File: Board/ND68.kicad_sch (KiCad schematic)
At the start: 4 parts

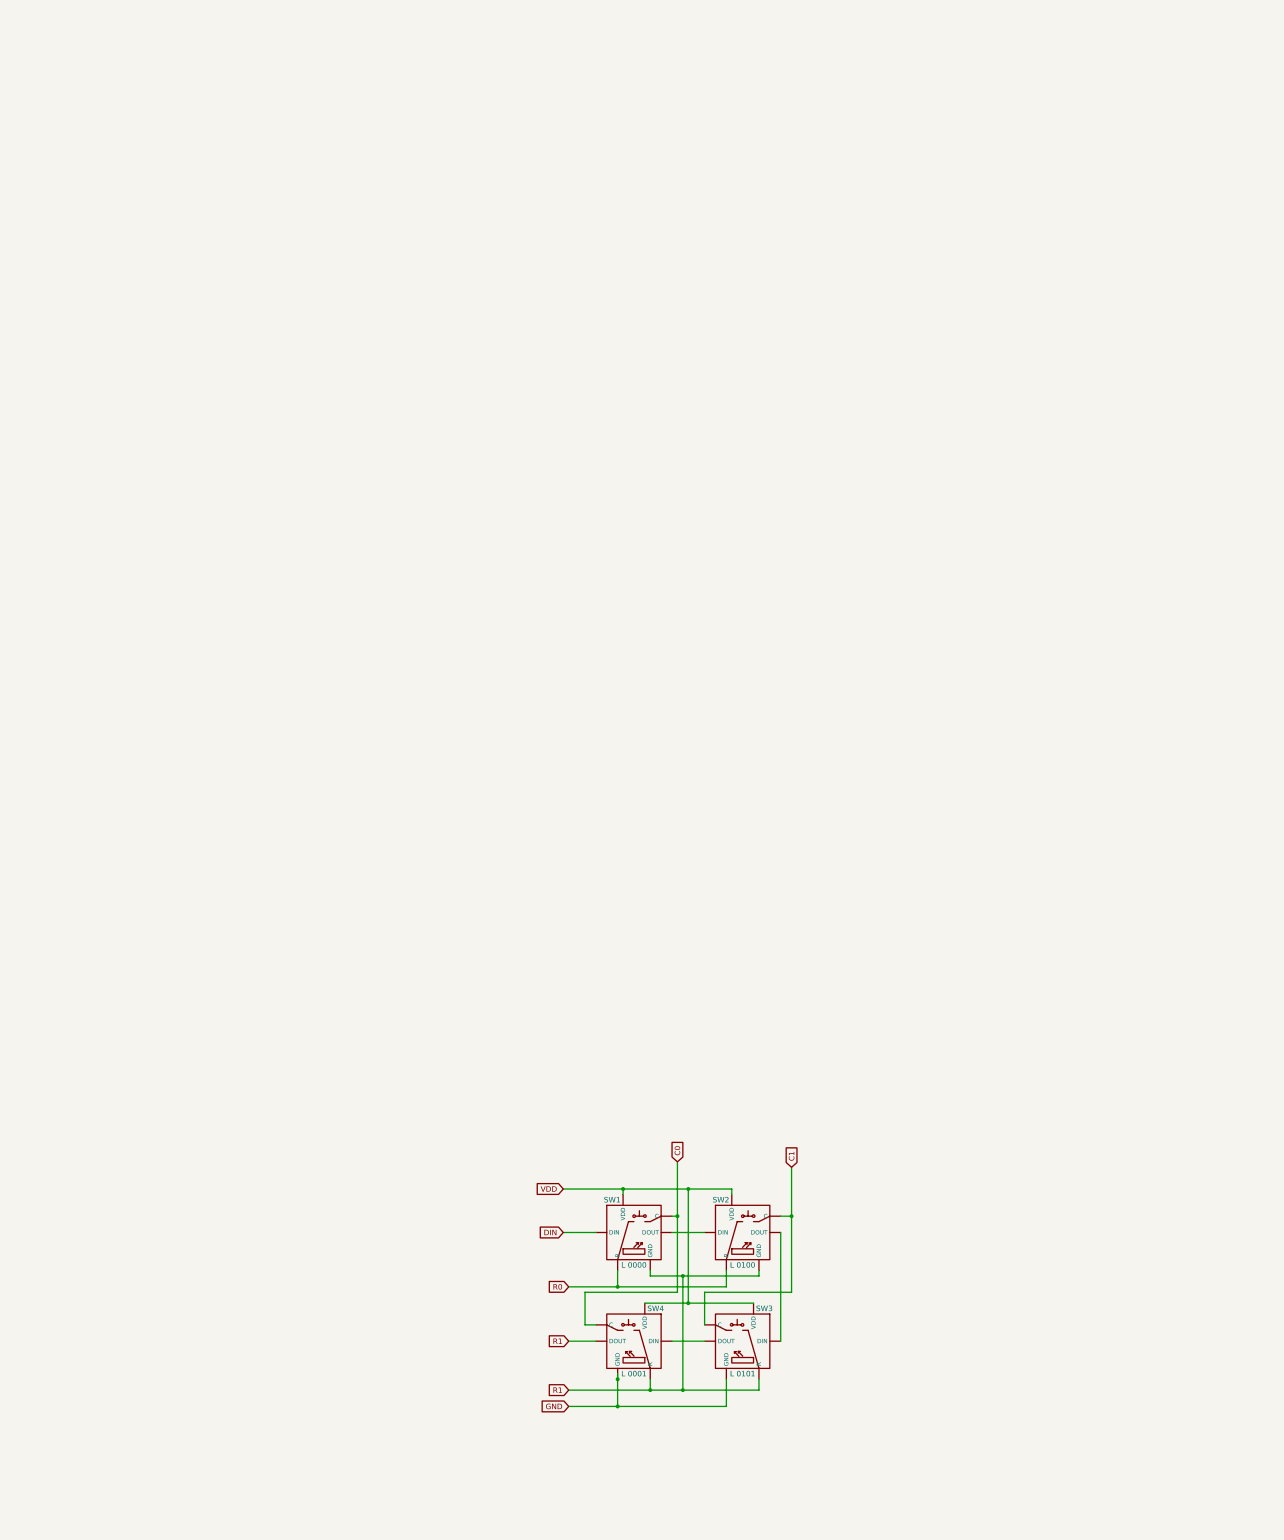
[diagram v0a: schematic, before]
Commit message: Added schematics, footprints, 3d models, and wiring to rp2040 input supply
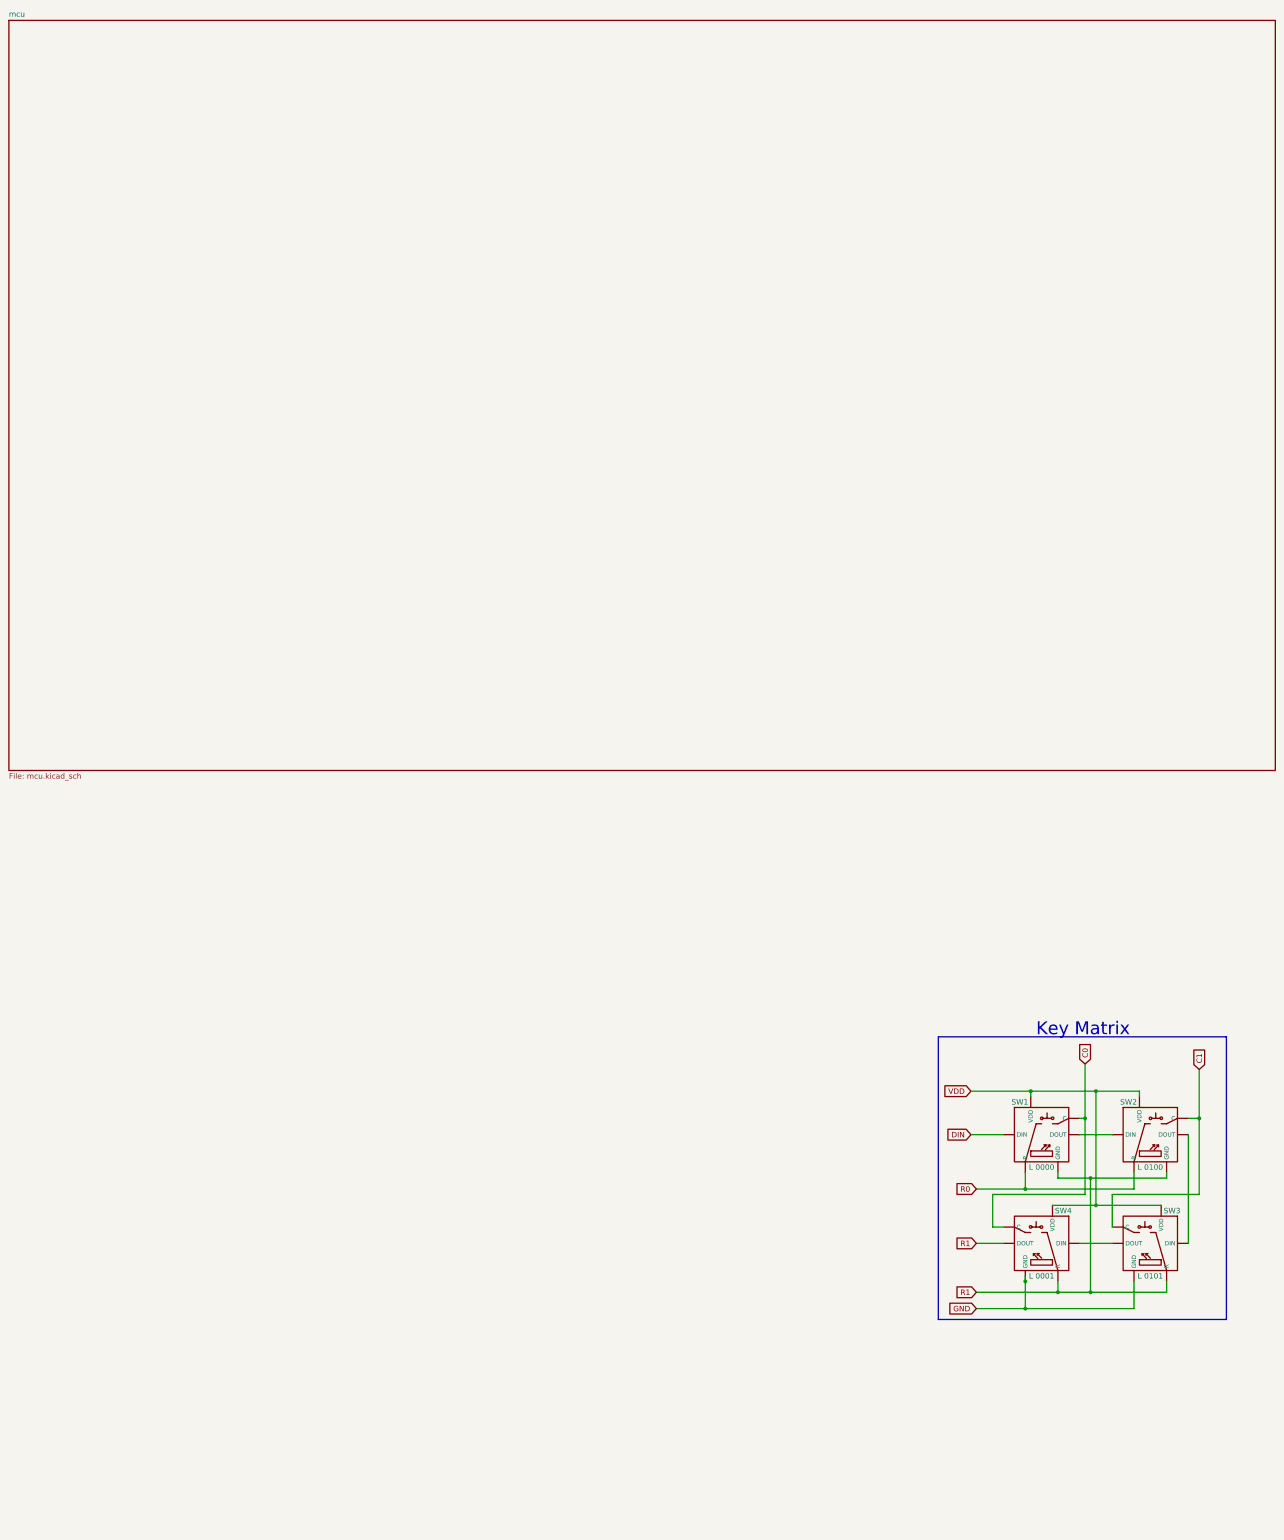
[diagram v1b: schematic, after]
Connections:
- new net: SW3. (VDD), SW4. (VDD)
- new net: SW2. (VDD), SW3. (VDD)
- new net: SW1. (VDD), SW2. (VDD)
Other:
- added sheet mcu (mcu.kicad_sch)
- note added: "Key Matrix"
- moved on the sheet: SW1, SW2, SW3, SW4

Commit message: renamed mcu sheet to usbc
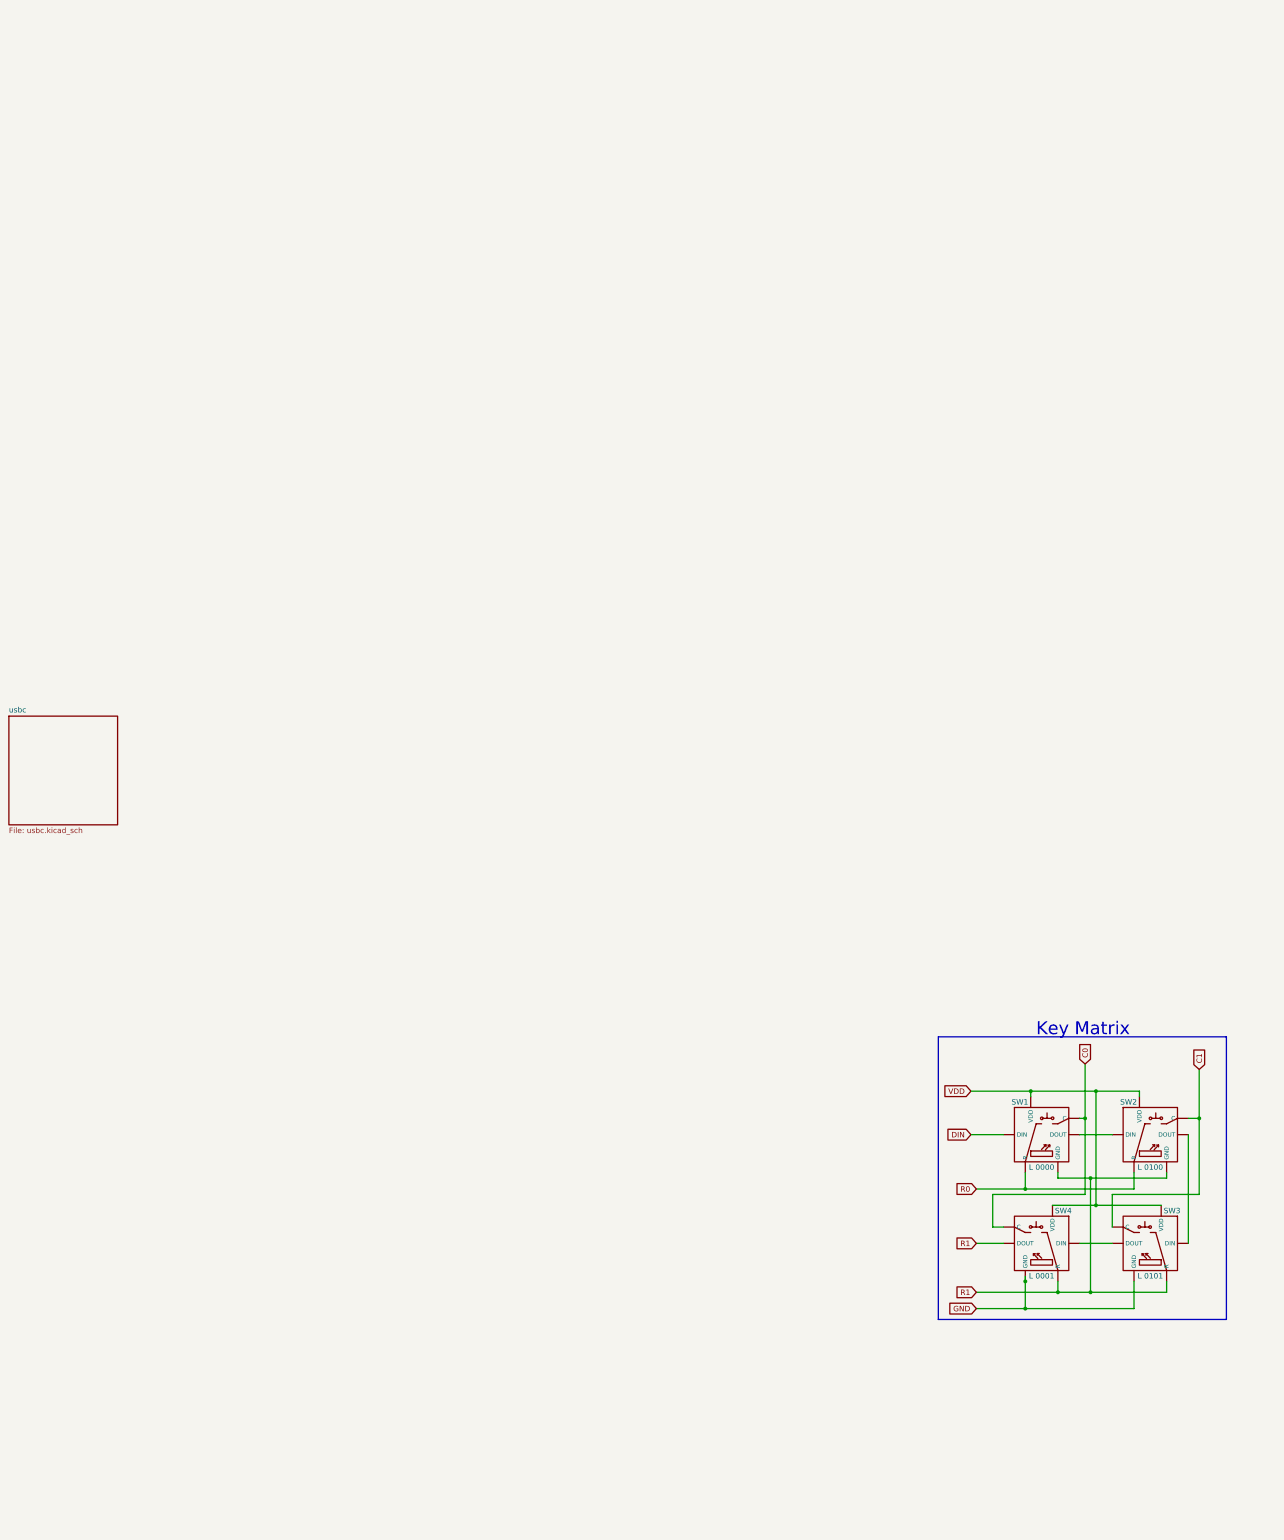
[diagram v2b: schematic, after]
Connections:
- new net: SW3. (VDD), SW4. (VDD)
- new net: SW2. (VDD), SW3. (VDD)
- new net: SW1. (VDD), SW2. (VDD)
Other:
- sheet mcu renamed usbc
- sheet usbc: file mcu.kicad_sch -> usbc.kicad_sch
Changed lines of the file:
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@@
     )
   )
-  (sheet (at 0 -213.36) (size 295.91 175.26) (fields_autoplaced)
+  (sheet (at 0 -50.8) (size 25.4 25.4) (fields_autoplaced)
     (stroke (width 0.1524) (type solid))
     (fill (color 0 0 0 0.0000))
-    (property "Sheetname" "mcu" (at 0 -214.0716 0)
+    (property "Sheetname" "usbc" (at 0 -51.5116 0)
       (effects (font (size 1.27 1.27)) (justify left bottom))
     )
-    (property "Sheetfile" "mcu.kicad_sch" (at 0 -37.5154 0)
+    (property "Sheetfile" "usbc.kicad_sch" (at 0 -24.8154 0)
       (effects (font (size 1.27 1.27)) (justify left top))
     )

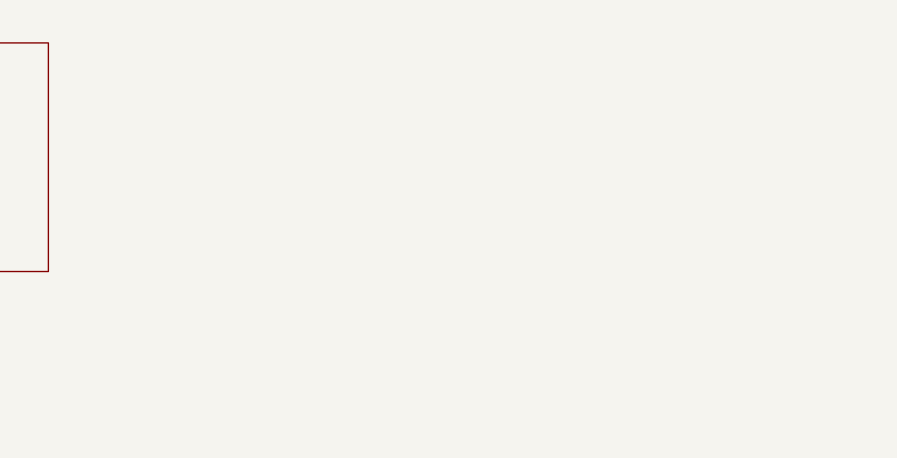
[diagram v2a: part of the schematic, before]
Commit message: Added mcu power pin decoupling capacitors
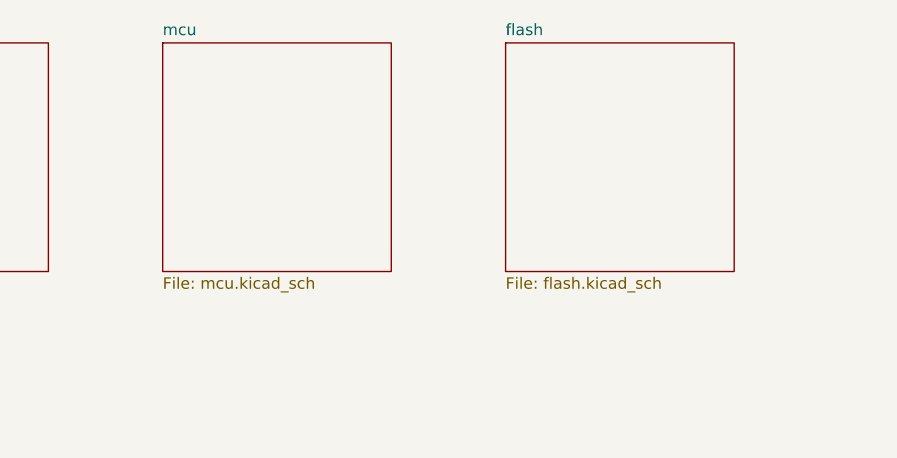
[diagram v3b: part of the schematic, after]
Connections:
- new net: SW3. (VDD), SW4. (VDD)
- new net: SW2. (VDD), SW3. (VDD)
- new net: SW1. (VDD), SW2. (VDD)
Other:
- added sheet flash (flash.kicad_sch)
- added sheet mcu (mcu.kicad_sch)
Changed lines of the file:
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@@
+    )
+  )
+  (sheet (at 76.2 -50.8) (size 25.4 25.4) (fields_autoplaced)
+    (stroke (width 0.1524) (type solid))
+    (fill (color 0 0 0 0.0000))
+    (property "Sheetname" "flash" (at 76.2 -51.5116 0)
+      (effects (font (size 1.27 1.27)) (justify left bottom))
+    )
+    (property "Sheetfile" "flash.kicad_sch" (at 76.2 -24.8154 0)
+      (effects (font (size 1.27 1.27)) (justify left top))
+    )
+    (instances
+      (project "ND68"
+        (path "/f6515d16-f8c0-46c5-adb6-b60d73ae282b" (page "4"))
+      )
+    )
+  )
+  (sheet (at 38.1 -50.8) (size 25.4 25.4) (fields_autoplaced)
+    (stroke (width 0.1524) (type solid))
+    (fill (color 0 0 0 0.0000))
+    (property "Sheetname" "mcu" (at 38.1 -51.5116 0)
+      (effects (font (size 1.27 1.27)) (justify left bottom))
+    )
+    (property "Sheetfile" "mcu.kicad_sch" (at 38.1 -24.8154 0)
+      (effects (font (size 1.27 1.27)) (justify left top))
+    )
+    (instances
+      (project "ND68"
+        (path "/f6515d16-f8c0-46c5-adb6-b60d73ae282b" (page "3"))
+      )
     )
   )

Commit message: Finished creating crystal oscillator
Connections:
- new net: SW3. (VDD), SW4. (VDD)
- new net: SW2. (VDD), SW3. (VDD)
- new net: SW1. (VDD), SW2. (VDD)
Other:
- added sheet crystal (crystal.kicad_sch)
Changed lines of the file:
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@@
+    )
+  )
+  (sheet (at 114.3 -50.8) (size 25.4 25.4) (fields_autoplaced)
+    (stroke (width 0.1524) (type solid))
+    (fill (color 0 0 0 0.0000))
+    (property "Sheetname" "crystal" (at 114.3 -51.5116 0)
+      (effects (font (size 1.27 1.27)) (justify left bottom))
+    )
+    (property "Sheetfile" "crystal.kicad_sch" (at 114.3 -24.8154 0)
+      (effects (font (size 1.27 1.27)) (justify left top))
+    )
+    (instances
+      (project "ND68"
+        (path "/f6515d16-f8c0-46c5-adb6-b60d73ae282b" (page "5"))
+      )
     )
   )

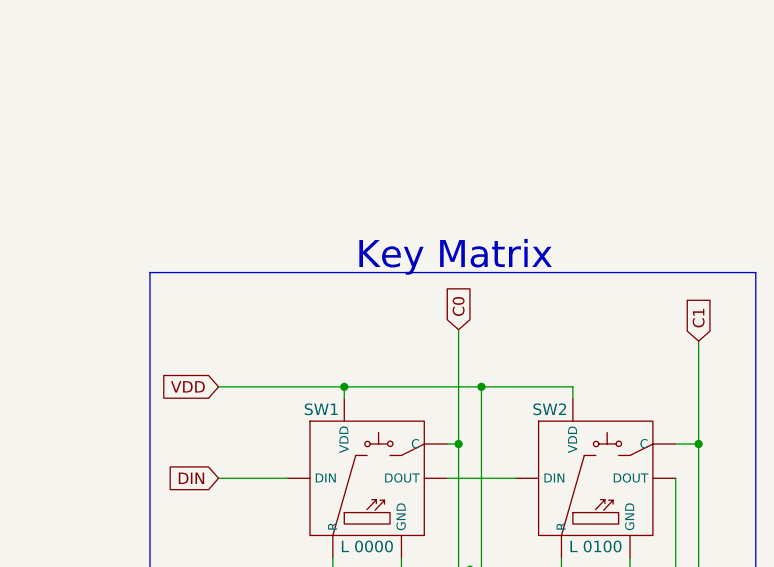
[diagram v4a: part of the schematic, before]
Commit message: Added the rest of the required stuff tp the mcu
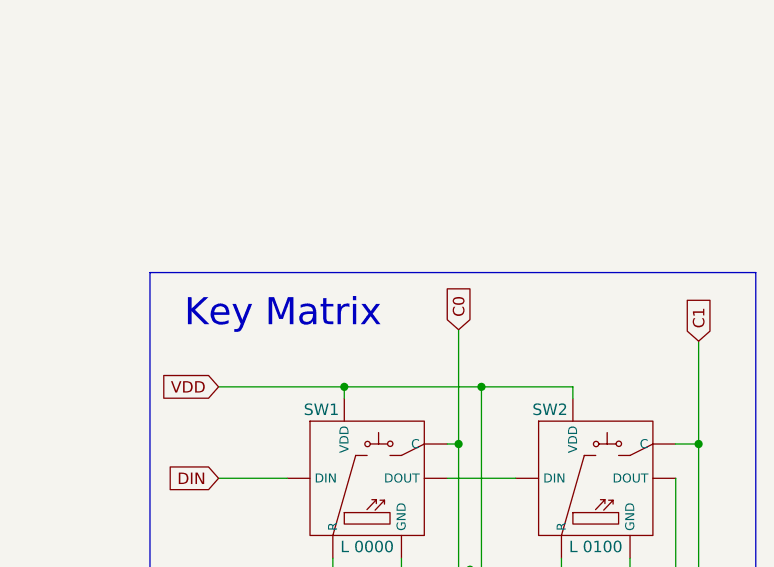
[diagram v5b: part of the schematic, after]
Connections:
- new net: SW3. (VDD), SW4. (VDD)
- new net: SW2. (VDD), SW3. (VDD)
- new net: SW1. (VDD), SW2. (VDD)
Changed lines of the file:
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@@
     (fill (type none))
   )
-  (text "Key Matrix" (at 240.03 24.13 0)
+  (text "Key Matrix" (at 220.98 30.48 0)
     (effects (font (size 3 3)) (justify left bottom))
   )
